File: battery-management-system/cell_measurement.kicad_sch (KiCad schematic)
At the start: 29 parts, among them Q13 BS250FTA, Q18 DMN3730U, Q5 DMN3730U, Q6 BS250FTA, Q7 BS250FTA, Q8 BS250FTA, Q9 BS250FTA, U10 LM2904M8-13, U6 LM2904M8-13, U7 LM2904M8-13

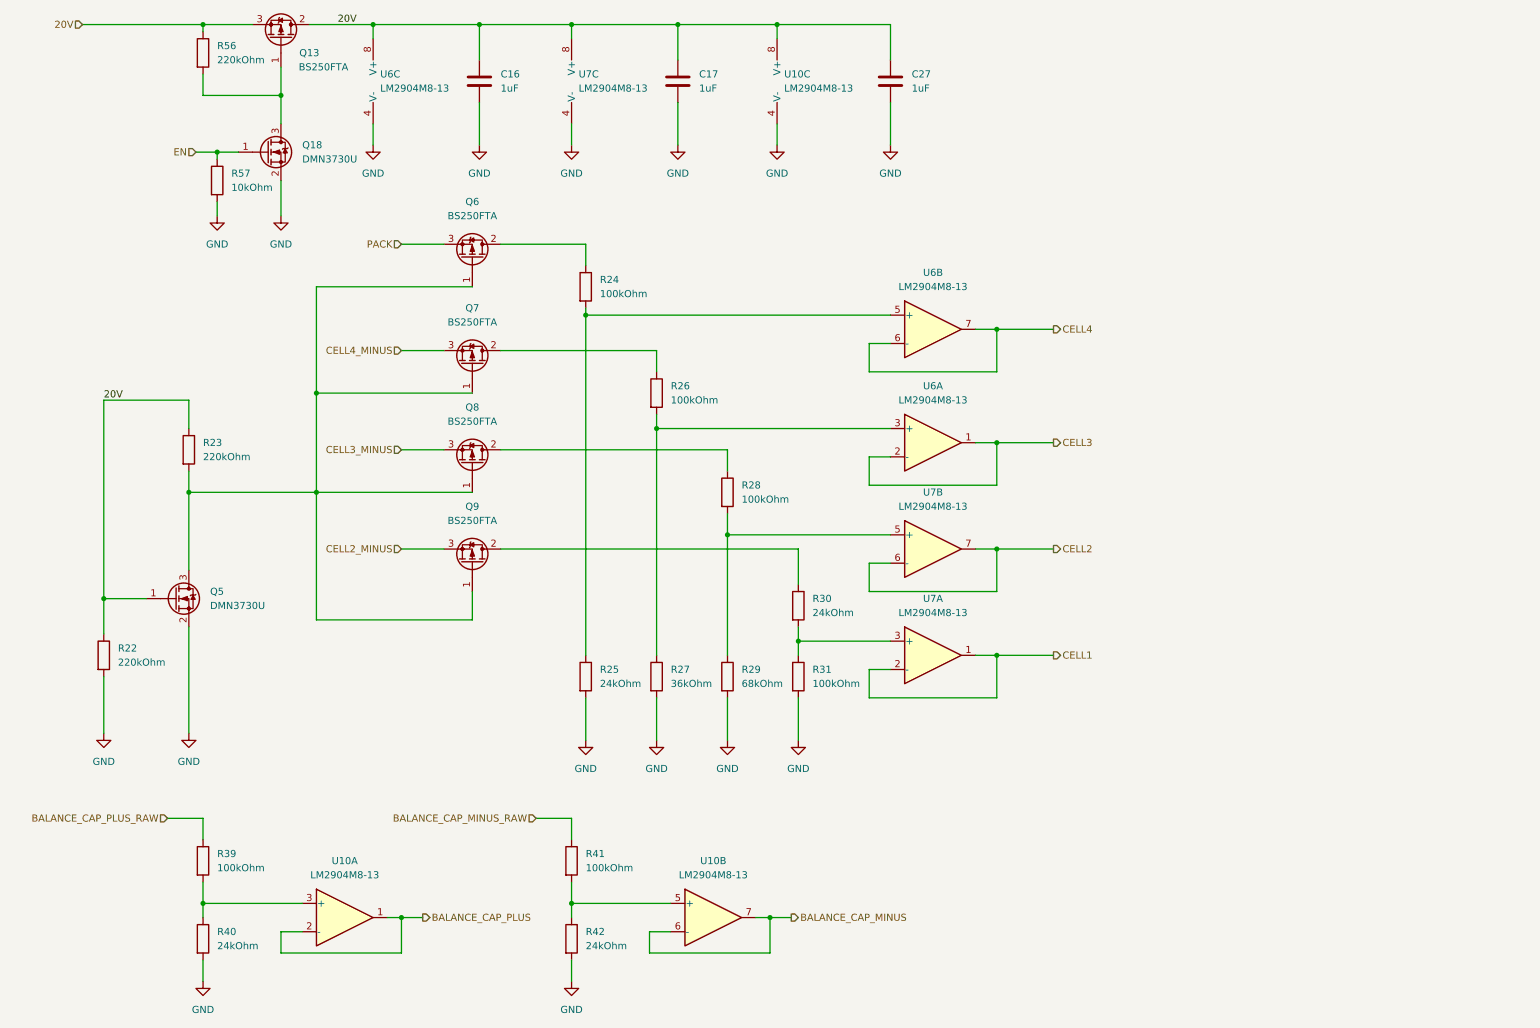
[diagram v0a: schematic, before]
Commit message: fix current sensing
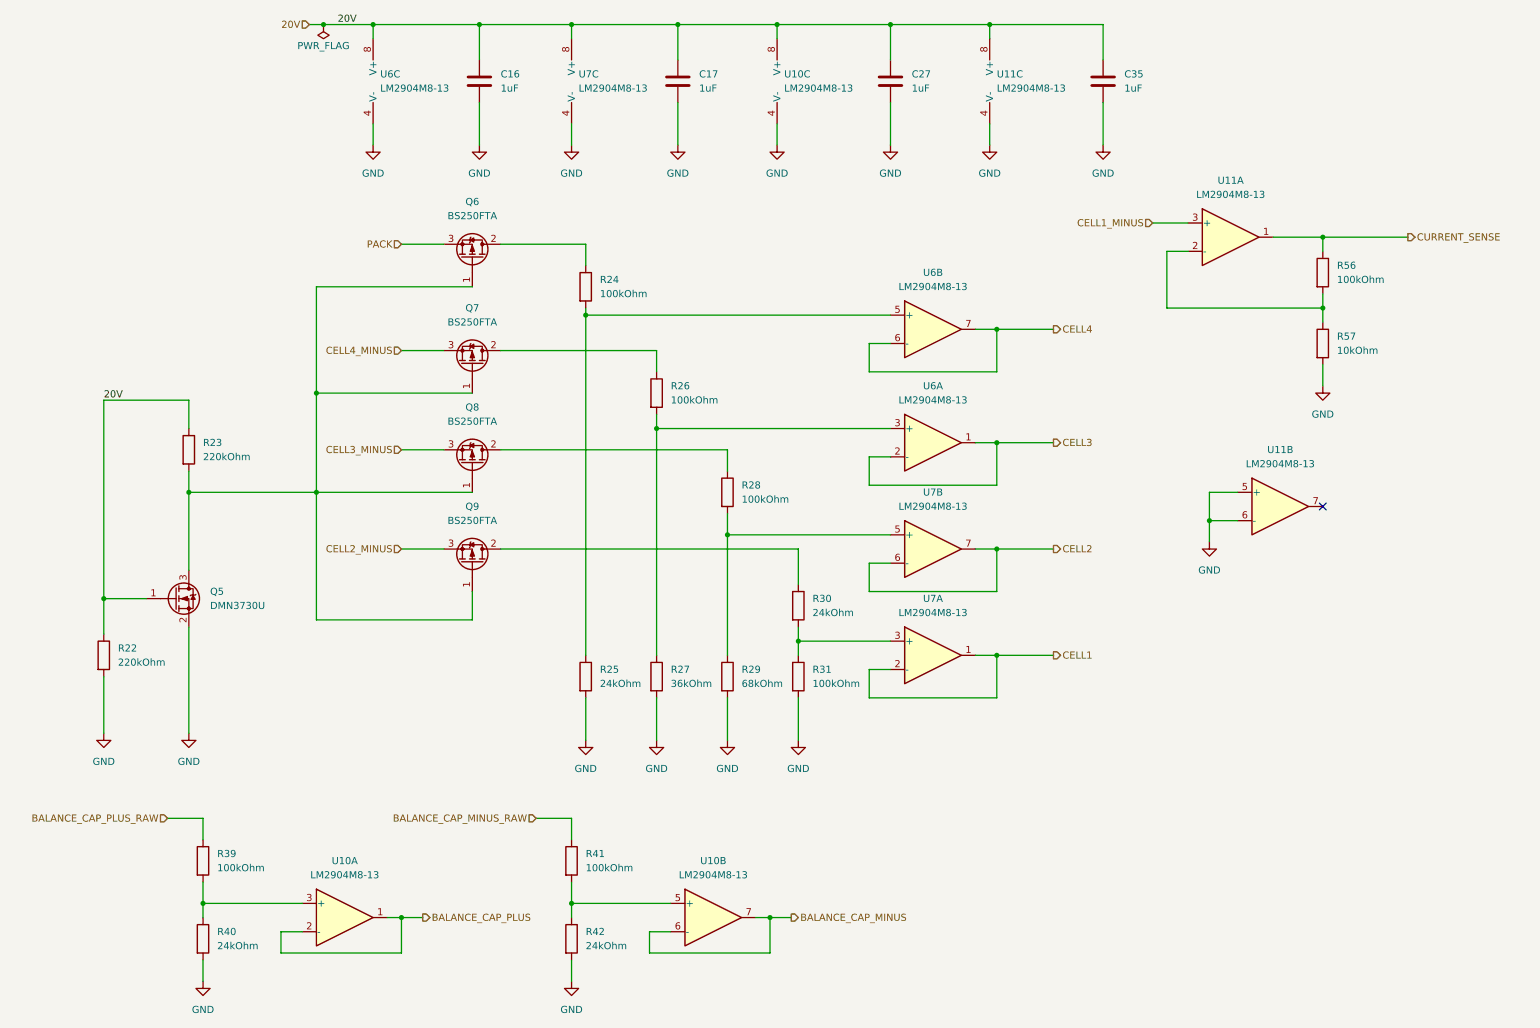
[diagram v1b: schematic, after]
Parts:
- removed Q13: BS250FTA, benediktibk:SOT-23, symbol benediktibk:BS250FTA
- removed Q18: DMN3730U, benediktibk:SOT-23, symbol benediktibk:DMN3730U
- removed R56: 220kOhm, benediktibk:R_0603_1608Metric_Pad0.98x0.95mm_HandSolder, symbol benediktibk:R_220kOhm_SMD_0603_100mW_1%
- added C35: 1uF, benediktibk:C_0603_1608Metric_Pad1.08x0.95mm_HandSolder, symbol benediktibk:C_1uF_SMD_0603_50V_10%
- added R56: 100kOhm, benediktibk:R_0603_1608Metric_Pad0.98x0.95mm_HandSolder, symbol benediktibk:R_100kOhm_SMD_0603_100mW_1%
- added U11: LM2904M8-13, benediktibk:MSOP-8_3x3mm_P0.65mm, symbol benediktibk:LM2904M8-13
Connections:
- net 20V: now also C35.1, U11.8 (V+)
- net GND: now also C35.2, U11.4 (V-), U11.5 (+), U11.6 (-)
- net EN: no longer names the net of R57.1
- net EN: now also R56.2, U11.2 (-)
- new net CELL1_MINUS: U11.3 (+)
- new net CURRENT_SENSE: R56.1, U11.1
- no-connect marks 0 -> 1

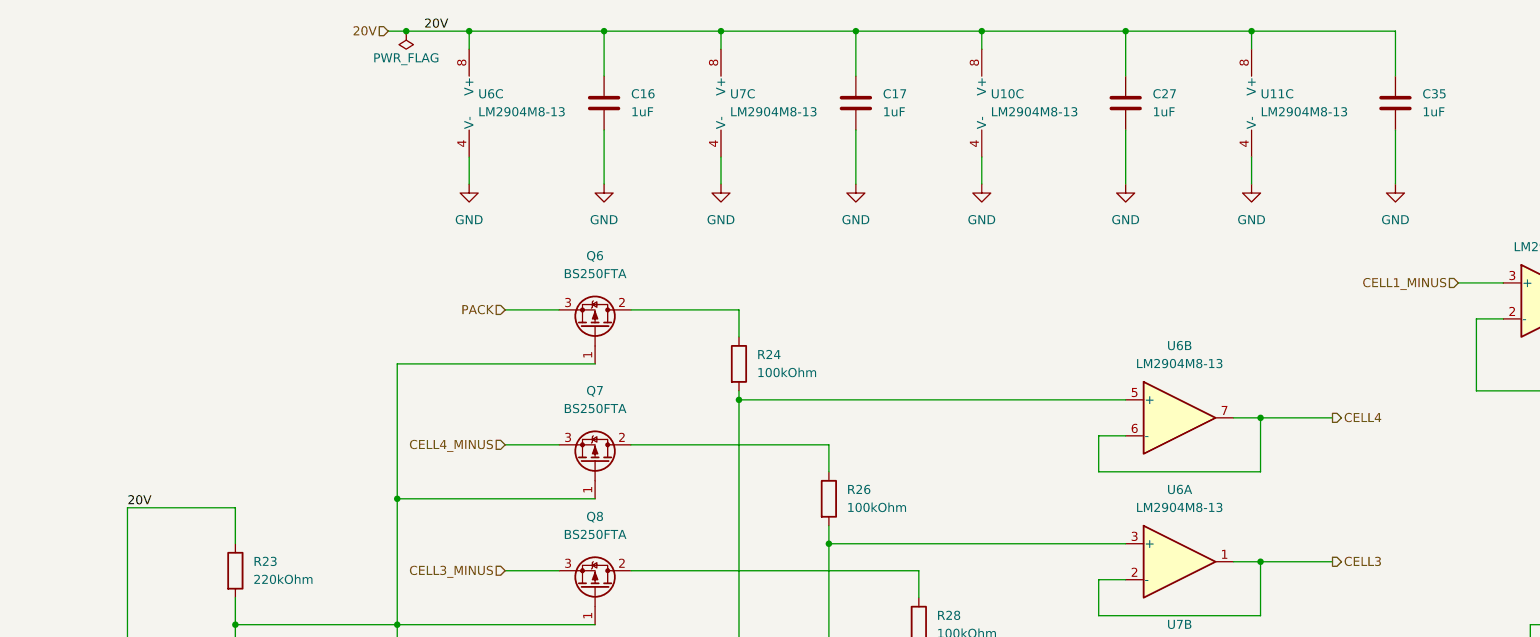
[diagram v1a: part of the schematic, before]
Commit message: add negative power supply for OPAMPs
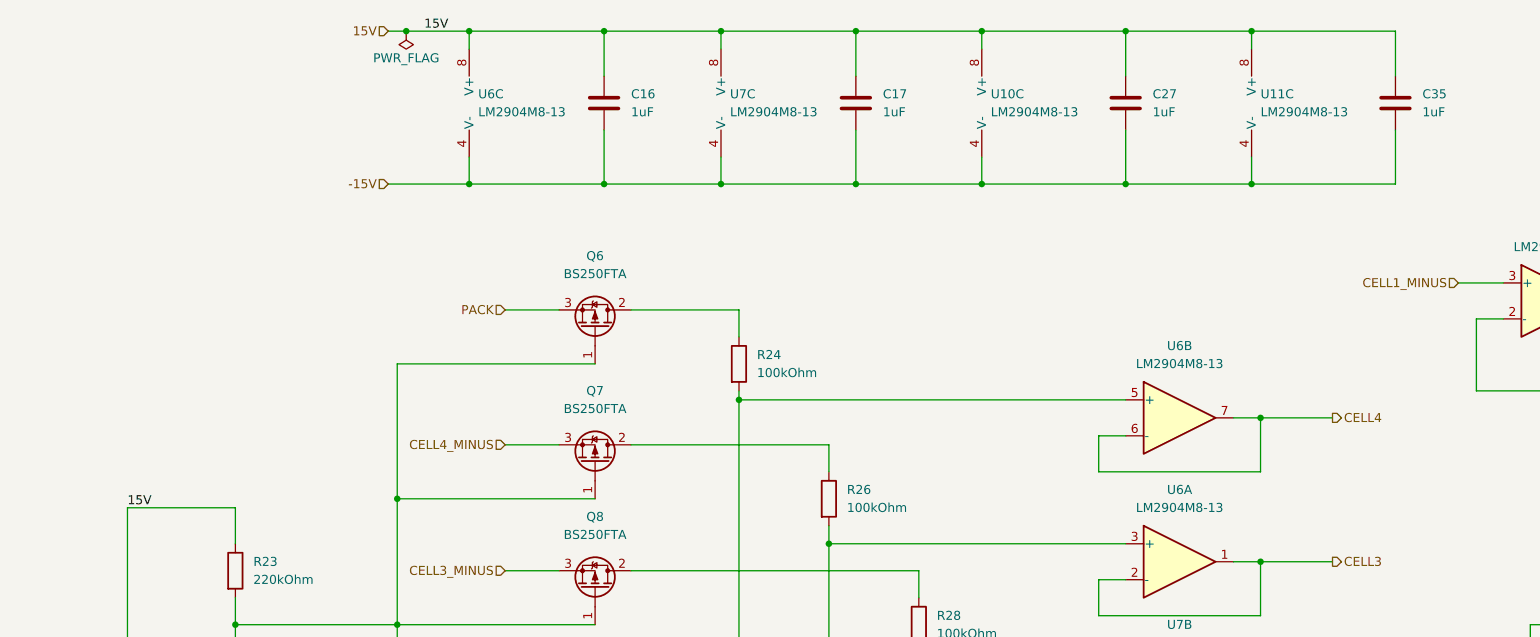
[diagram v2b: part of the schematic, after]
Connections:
- net GND: no longer C16.2, C17.2, C27.2, C35.2, U10.4 (V-), U11.4 (V-), U6.4 (V-), U7.4 (V-)
- net 20V renamed 15V
- new net -15V: C16.2, C17.2, C27.2, C35.2, U10.4 (V-), U11.4 (V-), U6.4 (V-), U7.4 (V-)

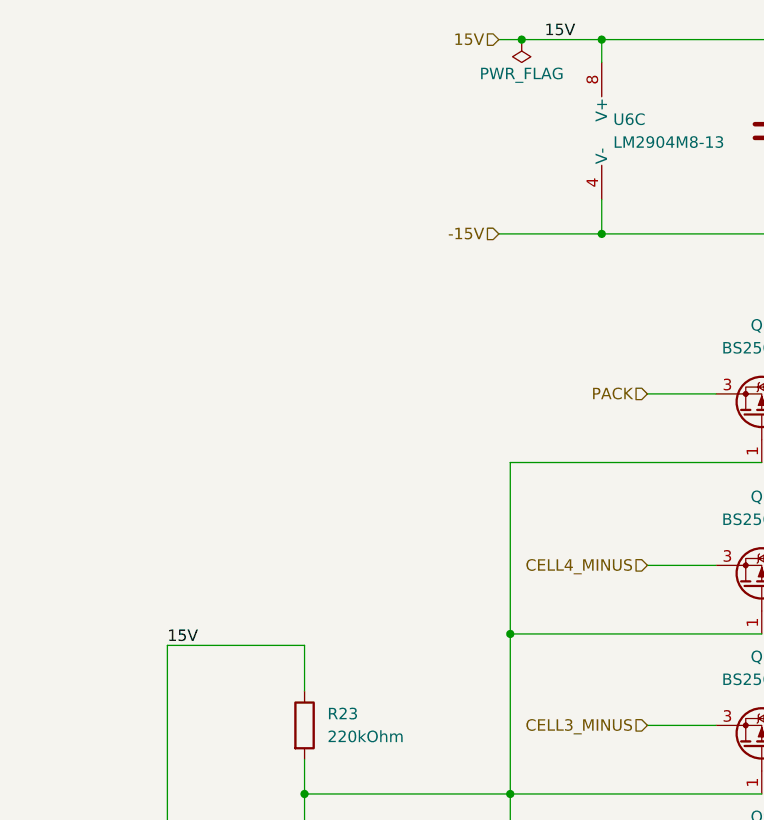
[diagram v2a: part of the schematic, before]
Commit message: implement negative power supply for OPAMPs
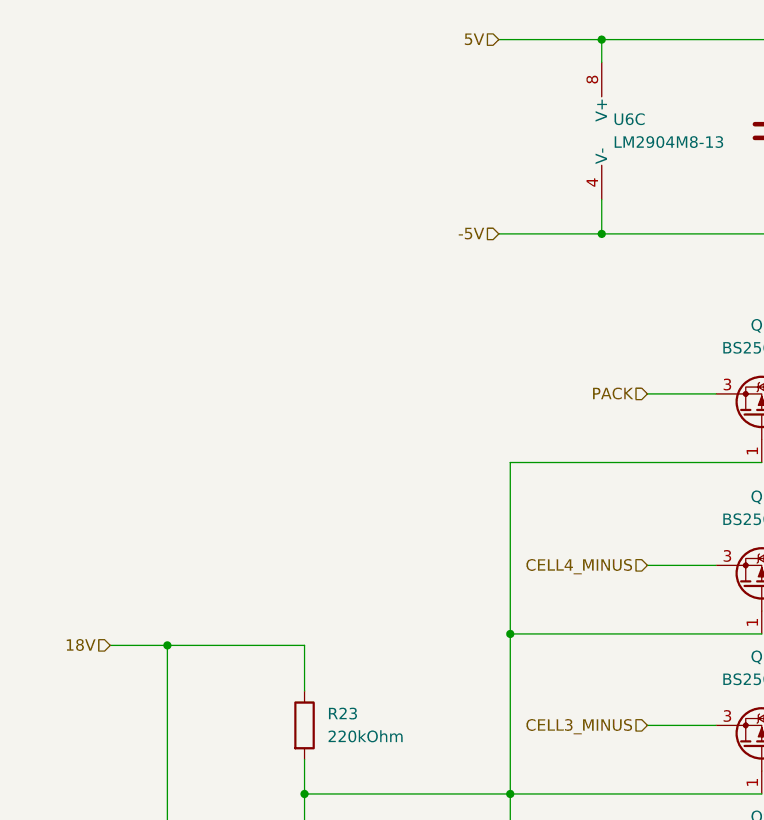
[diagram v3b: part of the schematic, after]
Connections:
- net -15V renamed -5V
- net 15V renamed 5V
- net 5V: no longer Q5.1 (G), R22.1, R23.1
- new net 18V: Q5.1 (G), R22.1, R23.1
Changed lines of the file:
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@@
   (junction (at 96.52 36.83) (diameter 0) (color 0 0 0 0)
   )
-  (junction (at 68.58 15.24) (diameter 0) (color 0 0 0 0)
-  )
   (junction (at 187.96 36.83) (diameter 0) (color 0 0 0 0)
   )
@@
   )
   (junction (at 113.03 15.24) (diameter 0) (color 0 0 0 0)
+  )
+  (junction (at 29.21 82.55) (diameter 0) (color 0 0 0 0)
   )
   (junction (at 247.65 66.04) (diameter 0) (color 0 0 0 0)
@@
     (stroke (width 0) (type default))
   )
+  (wire (pts (xy 22.86 82.55) (xy 29.21 82.55))
+    (stroke (width 0) (type default))
+  )
   (wire (pts (xy 77.47 36.83) (xy 96.52 36.83))
     (stroke (width 0) (type default))
@@
     (stroke (width 0) (type default))
   )
-  (wire (pts (xy 66.04 15.24) (xy 68.58 15.24))
+  (wire (pts (xy 66.04 15.24) (xy 77.47 15.24))
     (stroke (width 0) (type default))
   )
@@
     (stroke (width 0) (type default))
   )
-  (wire (pts (xy 68.58 15.24) (xy 77.47 15.24))
-    (stroke (width 0) (type default))
-  )
   (wire (pts (xy 67.31 81.28) (xy 67.31 99.06))
     (stroke (width 0) (type default))
@@
   (wire (pts (xy 77.47 33.02) (xy 77.47 36.83))
     (stroke (width 0) (type default))
-  )
-  (label "15V" (at 71.12 15.24 0) (fields_autoplaced)
-    (effects (font (size 1.27 1.27)) (justify left bottom))
-  )
-  (label "15V" (at 29.21 82.55 0) (fields_autoplaced)
-    (effects (font (size 1.27 1.27)) (justify left bottom))
   )
   (hierarchical_label "BALANCE_CAP_PLUS_RAW" (shape input) (at 40.64 157.48 180) (fields_autoplaced)
@@
     (effects (font (size 1.27 1.27)) (justify right))
   )
-  (hierarchical_label "15V" (shape input) (at 66.04 15.24 180) (fields_autoplaced)
+  (hierarchical_label "5V" (shape input) (at 66.04 15.24 180) (fields_autoplaced)
     (effects (font (size 1.27 1.27)) (justify right))
   )
@@
     (effects (font (size 1.27 1.27)) (justify left))
   )
+  (hierarchical_label "18V" (shape input) (at 22.86 82.55 180) (fields_autoplaced)
+    (effects (font (size 1.27 1.27)) (justify right))
+  )
   (hierarchical_label "CELL4_MINUS" (shape input) (at 82.55 73.66 180) (fields_autoplaced)
     (effects (font (size 1.27 1.27)) (justify right))
@@
     (effects (font (size 1.27 1.27)) (justify left))
   )
-  (hierarchical_label "-15V" (shape input) (at 66.04 36.83 180) (fields_autoplaced)
+  (hierarchical_label "-5V" (shape input) (at 66.04 36.83 180) (fields_autoplaced)
     (effects (font (size 1.27 1.27)) (justify right))
   )
@@
         )
       )
-    )
-  )
-  (symbol (lib_id "power:PWR_FLAG") (at 68.58 15.24 0) (mirror x) (unit 1)
-    (in_bom yes) (on_board yes) (dnp no)
-    (property "Reference" "#FLG01" (at 68.58 17.145 0)
-      (effects (font (size 1.27 1.27)) hide)
-    )
-    (property "Value" "PWR_FLAG" (at 68.58 19.05 0)
-      (effects (font (size 1.27 1.27)))
-    )
-    (property "Footprint" "" (at 68.58 15.24 0)
-      (effects (font (size 1.27 1.27)) hide)
-    )
-    (property "Datasheet" "~" (at 68.58 15.24 0)
-      (effects (font (size 1.27 1.27)) hide)
-    )
-    (pin "1")
-    (instances
-      (project "battery-management-system"
-        (path "/5272f0ff-3069-41a9-bca2-80beede8b4b2/b1377397-46a1-4623-af59-88e4e694ca35"
-          (reference "#FLG01") (unit 1)
-        )
-        (path "/5272f0ff-3069-41a9-bca2-80beede8b4b2/3d1e17ba-3c41-4767-81ce-6010cdb0d005"
-          (reference "#FLG04") (unit 1)
-        )
-      )

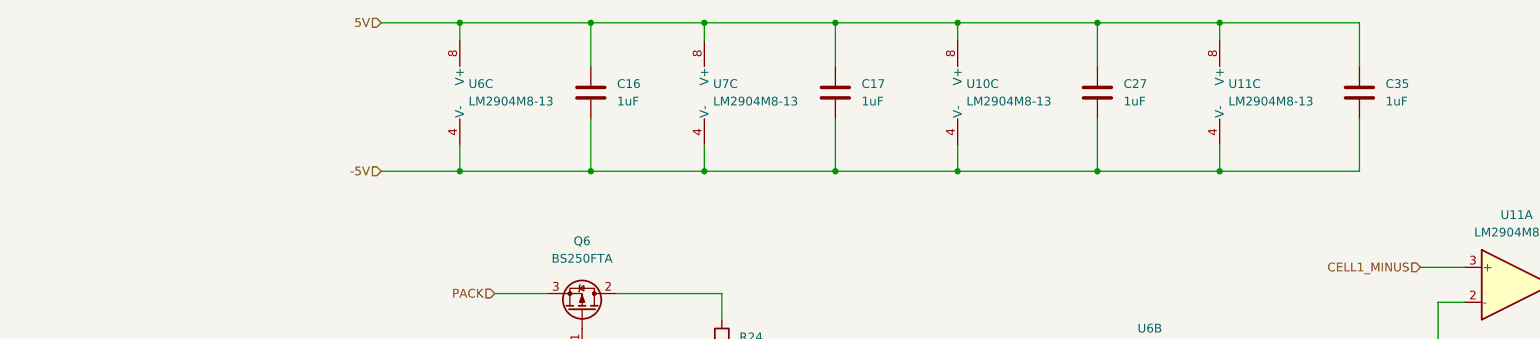
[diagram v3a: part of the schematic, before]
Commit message: fix ERC issues
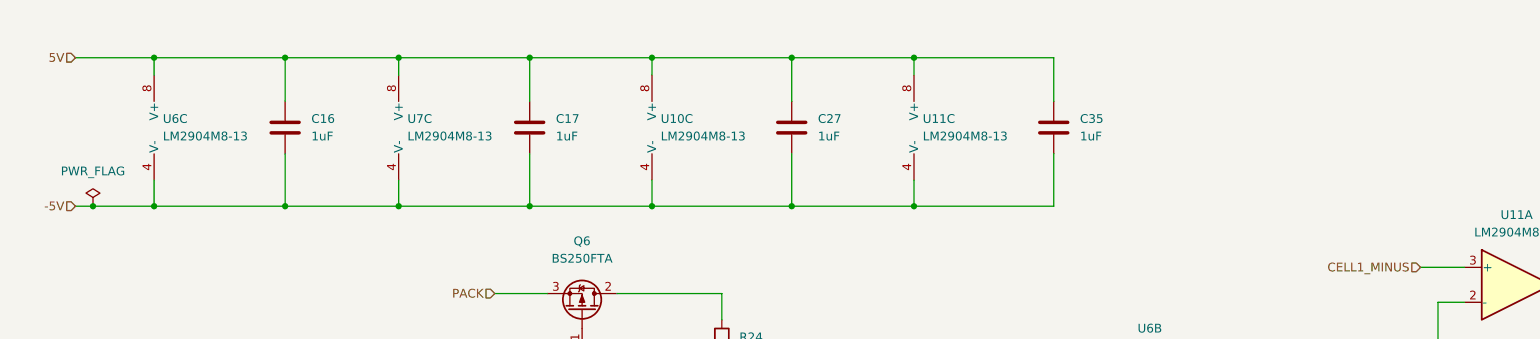
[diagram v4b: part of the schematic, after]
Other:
- moved on the sheet: C16, C17, C27, C35, U10C, U11C, U6C, U7C

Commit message: apply recommendations of Stefan
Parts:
- added C40, C41, C42, C43, C44, C45, C46, C47: 100nF, benediktibk:C_0603_1608Metric_Pad1.08x0.95mm_HandSolder, symbol benediktibk:C_100nF_SMD_0603_50V
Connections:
- net -5V: now also C41.2, C43.2, C45.2, C47.2
- net 5V: now also C40.1, C42.1, C44.1, C46.1
- net GND: now also C40.2, C41.1, C42.2, C43.1, C44.2, C45.1, C46.2, C47.1
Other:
- moved on the sheet: C16, C17, C27, C35, R56, R57, U10C, U11A, U11B, U11C, U7C

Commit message: improve layout
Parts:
- renumbered C40 to C33, C41 to C34, C16 to C35, C42 to C36, C43 to C37, C17 to C38, C44 to C39, C45 to C40, C27 to C41, C46 to C42, C47 to C43, C35 to C44, Q6 to Q10, Q7 to Q11, Q8 to Q12, Q9 to Q13, Q5 to Q9, R22 to R45, R23 to R46, R39 to R47, R40 to R48, R41 to R49, R42 to R50, R24 to R51, R25 to R52, R26 to R53, R27 to R54, R28 to R55, R29 to R56, R30 to R57, R31 to R58, R56 to R59, R57 to R60, U6 to U12, U10 to U13, U7 to U14, U11 to U15

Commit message: simplify cell measurement
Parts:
- removed C34, C37, C39, C40, C42, C43: 100nF, benediktibk:C_0603_1608Metric_Pad1.08x0.95mm_HandSolder, symbol benediktibk:C_100nF_SMD_0603_50V
- removed C41, C44: 1uF, benediktibk:C_0603_1608Metric_Pad1.08x0.95mm_HandSolder, symbol benediktibk:C_1uF_SMD_0603_50V_10%
- removed R47, R49, R59: 100kOhm, benediktibk:R_0603_1608Metric_Pad0.98x0.95mm_HandSolder, symbol benediktibk:R_100kOhm_SMD_0603_100mW_1%
- removed R48, R50: 24kOhm, benediktibk:R_0603_1608Metric_Pad0.98x0.95mm_HandSolder, symbol benediktibk:R_24kOhm_SMD_0603_100mW_1%
- removed R60: 10kOhm, benediktibk:R_0603_1608Metric_Pad0.98x0.95mm_HandSolder, symbol benediktibk:R_10kOhm_SMD_0603_100mW_1%
- removed U13, U15: LM2904M8-13, benediktibk:MSOP-8_3x3mm_P0.65mm, symbol benediktibk:LM2904M8-13
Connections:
- net -5V is gone; now on net GND: C35.2, C38.2, U12.4 (V-), U14.4 (V-)
- no-connect marks 1 -> 0
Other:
- moved on the sheet: C33, C36, C38
